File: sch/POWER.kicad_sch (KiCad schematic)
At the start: 35 parts, among them Q1 NTD2955T4G, Q2 IRLML0060, Q3 IRLML0060, U5 AP63205WU-7, U6 LD1117S33CTR

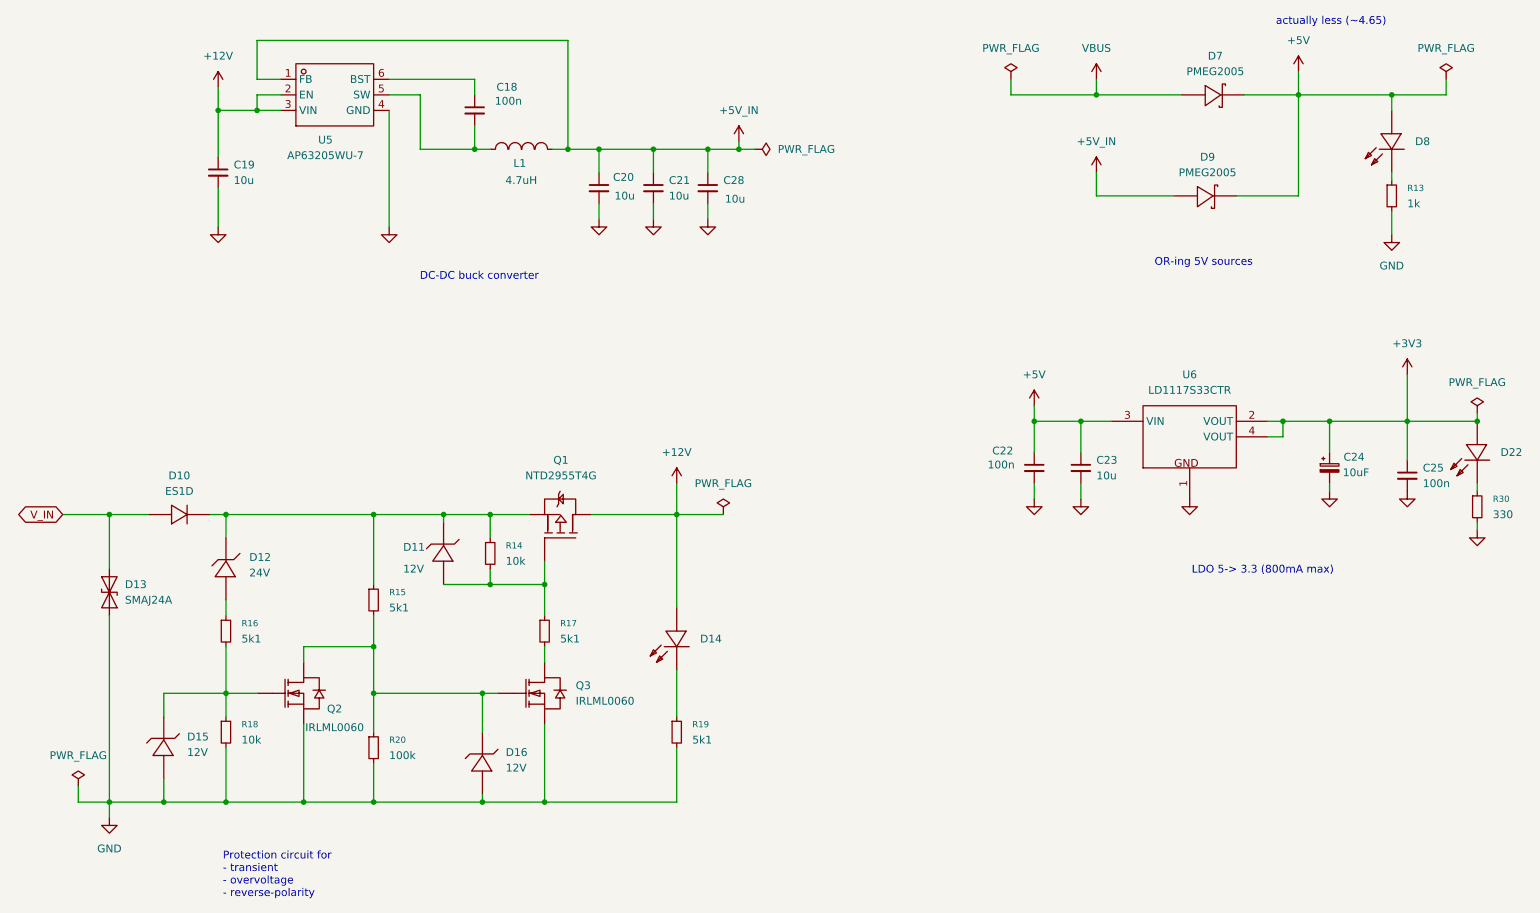
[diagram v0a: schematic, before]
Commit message: v1.1 changes * increase LED resistors as they are too bright * replace solder jumpers with pins * add corresponding 3D models
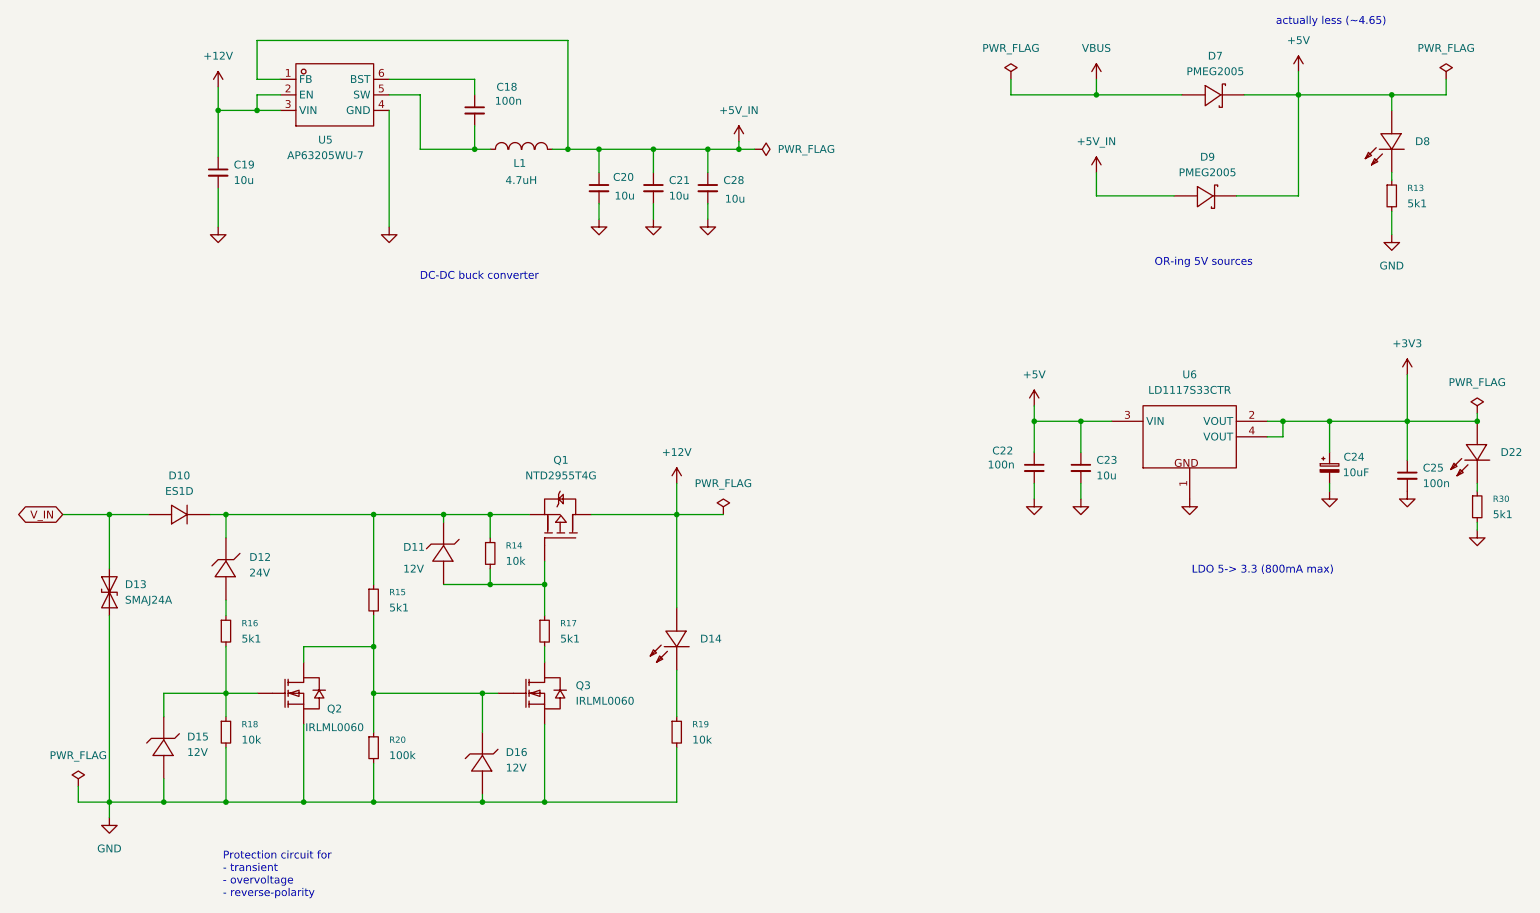
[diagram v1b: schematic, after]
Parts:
- R13: value 1k -> 5k1; Supplier Part C21190 -> C23186
- R19: value 5k1 -> 10k
- R30: value 330 -> 5k1; Supplier Part C23138 -> C23186
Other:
- title: 2CH CAN  Logger -> Dual Channel CAN Logger
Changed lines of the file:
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@@
 	(paper "A4")
 	(title_block
-		(title "2CH CAN  Logger")
-		(rev "1.0")
+		(title "Dual Channel CAN Logger")
+		(rev "1.1")
 	)
